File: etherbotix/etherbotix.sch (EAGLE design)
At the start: 107 parts, among them J1 J3011G21DNL, J2 22-03-5035, J3 22-03-5035, J4 22-03-5045, J5 22-03-5045, J6 1760510000, J7 1760490000, J8 502443-0470, J9 502443-0470, T1 TESTPAD, T2 TESTPAD, T3 TESTPAD, T4 TESTPAD, T5 TESTPAD, T6 TESTPAD, U1 STM32F407V, U2 TLK110, U3 OKI-78SR-5, U4 TLV1117, U5 ACS711ELCTR-25AB-T, U6 ACS711ELCTR-25AB-T, U7 MAX481CSA, U8 74LS126D, X1 25MHZ

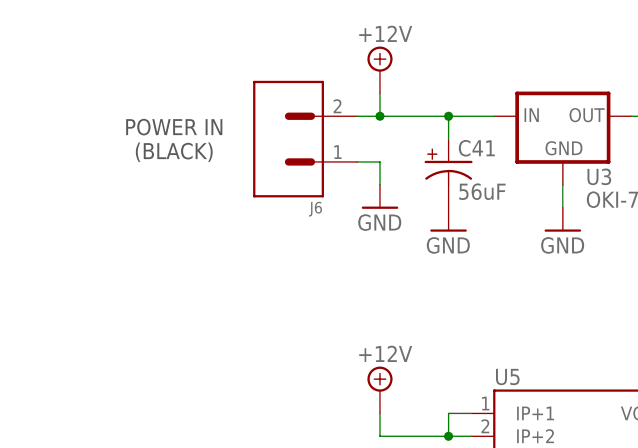
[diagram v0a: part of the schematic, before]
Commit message: add estop-capable 3-pin VIN header
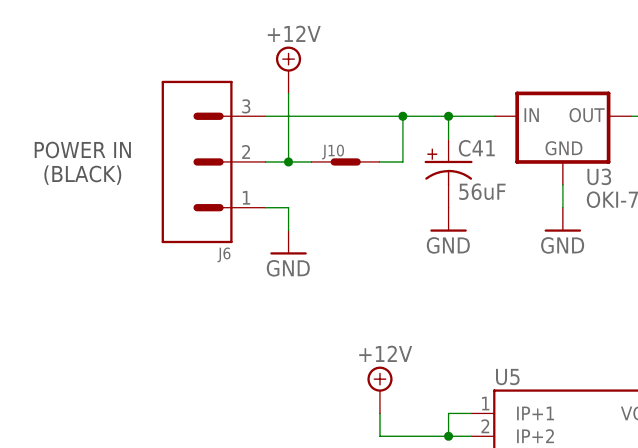
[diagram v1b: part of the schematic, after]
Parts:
- added J10: JUMPER, headers:JUMPER
- J6: value 1760510000 -> 1760520000; device headers:1760510000 -> headers:1760520000
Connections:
- new net N$29: C41.+, J10.B, J6.3, U3.IN
- net +12V: now also J10.A; no longer C41.+, U3.IN
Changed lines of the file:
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@@
 <part name="J4" library="molex" deviceset="22-03-5045" device=""/>
 <part name="J5" library="molex" deviceset="22-03-5045" device=""/>
-<part name="J6" library="headers" deviceset="1760510000" device=""/>
 <part name="J7" library="headers" deviceset="1760490000" device=""/>
 <part name="GND7" library="fergs" deviceset="GND" device=""/>
@@
 <part name="T5" library="fergs" deviceset="TESTPAD" device=""/>
 <part name="T6" library="fergs" deviceset="TESTPAD" device=""/>
+<part name="J6" library="headers" deviceset="1760520000" device=""/>
+<part name="J10" library="headers" deviceset="JUMPER" device=""/>
 </parts>
 <sheets>
 <sheet>
 <plain>
-<text x="15.24" y="205.74" size="1.778" layer="97" align="center">POWER IN
+<text x="5.08" y="203.2" size="1.778" layer="97" align="center">POWER IN
 (BLACK)</text>
 <text x="15.24" y="160.02" size="1.778" layer="97" align="center">AUX. OUT
@@
 <instance part="IMU" gate="G$1" x="314.96" y="25.4"/>
 <instance part="JTAG" gate="G$1" x="160.02" y="185.42"/>
-<instance part="SUPPLY1" gate="+12V" x="38.1" y="213.36"/>
+<instance part="SUPPLY1" gate="+12V" x="27.94" y="213.36"/>
 <instance part="SUPPLY2" gate="+5V" x="68.58" y="213.36"/>
 <instance part="SUPPLY3" gate="G$1" x="142.24" y="213.36"/>
-<instance part="GND1" gate="1" x="38.1" y="198.12"/>
+<instance part="GND1" gate="1" x="27.94" y="193.04"/>
 <instance part="GND2" gate="1" x="101.6" y="195.58"/>
 <instance part="GND3" gate="1" x="180.34" y="0"/>
@@
 <instance part="J4" gate="G$1" x="464.82" y="83.82"/>
 <instance part="J5" gate="G$1" x="495.3" y="83.82"/>
-<instance part="J6" gate="G$1" x="27.94" y="205.74" rot="R180"/>
 <instance part="J7" gate="G$1" x="27.94" y="160.02" rot="R180"/>
 <instance part="GND7" gate="1" x="58.42" y="195.58"/>
@@
 <instance part="T5" gate="G$1" x="325.12" y="154.94"/>
 <instance part="T6" gate="G$1" x="325.12" y="152.4"/>
+<instance part="J6" gate="G$1" x="17.78" y="203.2" rot="R180"/>
+<instance part="J10" gate="G$1" x="33.02" y="203.2"/>
 </instances>
 <busses>
@@
 <net name="+12V" class="0">
 <segment>
+<wire x1="25.4" y1="203.2" x2="27.94" y2="203.2" width="0.1524" layer="91"/>
+<pinref part="SUPPLY1" gate="+12V" pin="+12V"/>
+<wire x1="27.94" y1="203.2" x2="27.94" y2="210.82" width="0.1524" layer="91"/>
 <pinref part="J6" gate="G$1" pin="2"/>
-<pinref part="U3" gate="G$1" pin="IN"/>
-<wire x1="35.56" y1="208.28" x2="38.1" y2="208.28" width="0.1524" layer="91"/>
-<pinref part="SUPPLY1" gate="+12V" pin="+12V"/>
-<wire x1="38.1" y1="208.28" x2="45.72" y2="208.28" width="0.1524" layer="91"/>
-<wire x1="45.72" y1="208.28" x2="50.8" y2="208.28" width="0.1524" layer="91"/>
-<wire x1="38.1" y1="208.28" x2="38.1" y2="210.82" width="0.1524" layer="91"/>
-<junction x="38.1" y="208.28"/>
-<pinref part="C41" gate="G$1" pin="+"/>
-<wire x1="45.72" y1="205.74" x2="45.72" y2="208.28" width="0.1524" layer="91"/>
-<junction x="45.72" y="208.28"/>
+<wire x1="27.94" y1="203.2" x2="30.48" y2="203.2" width="0.1524" layer="91"/>
+<junction x="27.94" y="203.2"/>
+<pinref part="J10" gate="G$1" pin="A"/>
 </segment>
 <segment>
@@
 <net name="GND" class="0">
 <segment>
+<wire x1="25.4" y1="198.12" x2="27.94" y2="198.12" width="0.1524" layer="91"/>
+<wire x1="27.94" y1="198.12" x2="27.94" y2="195.58" width="0.1524" layer="91"/>
+<pinref part="GND1" gate="1" pin="GND"/>
 <pinref part="J6" gate="G$1" pin="1"/>
-<wire x1="35.56" y1="203.2" x2="38.1" y2="203.2" width="0.1524" layer="91"/>
-<wire x1="38.1" y1="203.2" x2="38.1" y2="200.66" width="0.1524" layer="91"/>
-<pinref part="GND1" gate="1" pin="GND"/>
 </segment>
 <segment>
@@
 </segment>
 </net>
+<net name="N$29" class="0">
+<segment>
+<pinref part="U3" gate="G$1" pin="IN"/>
+<wire x1="45.72" y1="208.28" x2="50.8" y2="208.28" width="0.1524" layer="91"/>
+<pinref part="C41" gate="G$1" pin="+"/>
+<wire x1="45.72" y1="205.74" x2="45.72" y2="208.28" width="0.1524" layer="91"/>
+<pinref part="J6" gate="G$1" pin="3"/>
+<wire x1="25.4" y1="208.28" x2="40.64" y2="208.28" width="0.1524" layer="91"/>
+<junction x="45.72" y="208.28"/>
+<wire x1="40.64" y1="208.28" x2="45.72" y2="208.28" width="0.1524" layer="91"/>
+<wire x1="40.64" y1="208.28" x2="40.64" y2="203.2" width="0.1524" layer="91"/>
+<junction x="40.64" y="208.28"/>
+<wire x1="40.64" y1="203.2" x2="38.1" y2="203.2" width="0.1524" layer="91"/>
+<pinref part="J10" gate="G$1" pin="B"/>
+</segment>
+</net>

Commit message: start rev. B
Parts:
- added T7, T8, T9: TESTPAD, fergs:TESTPAD
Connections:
- new net PE0: T7.1, U1.PE0(5T)
- new net PE1: T8.1, U1.PE1(5T)
- new net PE4: T9.1, U1.PE4(5T)
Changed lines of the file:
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@@
 <part name="J6" library="headers" deviceset="1760520000" device=""/>
 <part name="J10" library="headers" deviceset="JUMPER" device=""/>
+<part name="T7" library="fergs" deviceset="TESTPAD" device=""/>
+<part name="T8" library="fergs" deviceset="TESTPAD" device=""/>
+<part name="T9" library="fergs" deviceset="TESTPAD" device=""/>
 </parts>
 <sheets>
@@
 <instance part="J6" gate="G$1" x="17.78" y="203.2" rot="R180"/>
 <instance part="J10" gate="G$1" x="33.02" y="203.2"/>
+<instance part="T7" gate="G$1" x="325.12" y="114.3"/>
+<instance part="T8" gate="G$1" x="325.12" y="111.76"/>
+<instance part="T9" gate="G$1" x="325.12" y="104.14"/>
 </instances>
 <busses>
@@
 </segment>
 </net>
+<net name="PE4" class="0">
+<segment>
+<pinref part="U1" gate="G$1" pin="PE4(5T)"/>
+<pinref part="T9" gate="G$1" pin="1"/>
+<wire x1="322.58" y1="104.14" x2="317.5" y2="104.14" width="0.1524" layer="91"/>
+</segment>
+</net>
+<net name="PE1" class="0">
+<segment>
+<pinref part="U1" gate="G$1" pin="PE1(5T)"/>
+<pinref part="T8" gate="G$1" pin="1"/>
+<wire x1="322.58" y1="111.76" x2="317.5" y2="111.76" width="0.1524" layer="91"/>
+</segment>
+</net>
+<net name="PE0" class="0">
+<segment>
+<pinref part="U1" gate="G$1" pin="PE0(5T)"/>
+<pinref part="T7" gate="G$1" pin="1"/>
+<wire x1="322.58" y1="114.3" x2="317.5" y2="114.3" width="0.1524" layer="91"/>
+</segment>
+</net>

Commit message: add testpads to clocks, encoders, current sense
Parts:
- added T10, T11, T12, T13, T14, T15, T16, T17: TESTPAD, fergs:TESTPAD
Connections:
- net AUX_CURRENT_SENSE: now also T17.1
- net ETH_CLK: now also T10.1
- net M1_ENC_A: now also T12.1
- net M1_ENC_B: now also T13.1
- net M2_ENC_A: now also T14.1
- net M2_ENC_B: now also T15.1
- net N$15: now also T11.1
- net SERVO_CURRENT_SENSE: now also T16.1
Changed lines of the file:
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@@
 <part name="T8" library="fergs" deviceset="TESTPAD" device=""/>
 <part name="T9" library="fergs" deviceset="TESTPAD" device=""/>
+<part name="T10" library="fergs" deviceset="TESTPAD" device=""/>
+<part name="T11" library="fergs" deviceset="TESTPAD" device=""/>
+<part name="T12" library="fergs" deviceset="TESTPAD" device=""/>
+<part name="T13" library="fergs" deviceset="TESTPAD" device=""/>
+<part name="T14" library="fergs" deviceset="TESTPAD" device=""/>
+<part name="T15" library="fergs" deviceset="TESTPAD" device=""/>
+<part name="T16" library="fergs" deviceset="TESTPAD" device=""/>
+<part name="T17" library="fergs" deviceset="TESTPAD" device=""/>
 </parts>
 <sheets>
@@
 <instance part="T8" gate="G$1" x="325.12" y="111.76"/>
 <instance part="T9" gate="G$1" x="325.12" y="104.14"/>
+<instance part="T10" gate="G$1" x="55.88" y="119.38"/>
+<instance part="T11" gate="G$1" x="353.06" y="71.12"/>
+<instance part="T12" gate="G$1" x="365.76" y="195.58" rot="R180"/>
+<instance part="T13" gate="G$1" x="365.76" y="190.5" rot="R180"/>
+<instance part="T14" gate="G$1" x="365.76" y="157.48" rot="R180"/>
+<instance part="T15" gate="G$1" x="365.76" y="152.4" rot="R180"/>
+<instance part="T16" gate="G$1" x="515.62" y="121.92"/>
+<instance part="T17" gate="G$1" x="106.68" y="170.18"/>
 </instances>
 <busses>
@@
 <wire x1="73.66" y1="170.18" x2="104.14" y2="170.18" width="0.1524" layer="91"/>
 <label x="76.2" y="170.18" size="1.778" layer="95"/>
+<pinref part="T17" gate="G$1" pin="1"/>
 </segment>
 <segment>
@@
 <wire x1="477.52" y1="121.92" x2="513.08" y2="121.92" width="0.1524" layer="91"/>
 <label x="480.06" y="121.92" size="1.778" layer="95"/>
+<pinref part="T16" gate="G$1" pin="1"/>
 </segment>
 <segment>
@@
 <junction x="386.08" y="157.48"/>
 <pinref part="C18" gate="G$1" pin="1"/>
+<pinref part="T14" gate="G$1" pin="1"/>
 </segment>
 <segment>
@@
 <junction x="375.92" y="152.4"/>
 <pinref part="C17" gate="G$1" pin="1"/>
+<pinref part="T15" gate="G$1" pin="1"/>
 </segment>
 <segment>
@@
 <junction x="386.08" y="195.58"/>
 <pinref part="C13" gate="G$1" pin="1"/>
+<pinref part="T12" gate="G$1" pin="1"/>
 </segment>
 <segment>
@@
 <junction x="375.92" y="190.5"/>
 <pinref part="C4" gate="G$1" pin="1"/>
+<pinref part="T13" gate="G$1" pin="1"/>
 </segment>
 <segment>
@@
 <wire x1="347.98" y1="58.42" x2="347.98" y2="60.96" width="0.1524" layer="91"/>
 <junction x="347.98" y="60.96"/>
+<pinref part="T11" gate="G$1" pin="1"/>
+<wire x1="347.98" y1="71.12" x2="350.52" y2="71.12" width="0.1524" layer="91"/>
+<junction x="347.98" y="71.12"/>
 </segment>
 </net>
@@
 <wire x1="38.1" y1="119.38" x2="53.34" y2="119.38" width="0.1524" layer="91"/>
 <label x="40.64" y="119.38" size="1.778" layer="95"/>
-</segment>
-<segment>
+<pinref part="T10" gate="G$1" pin="1"/>
+</segment>
+<segment>

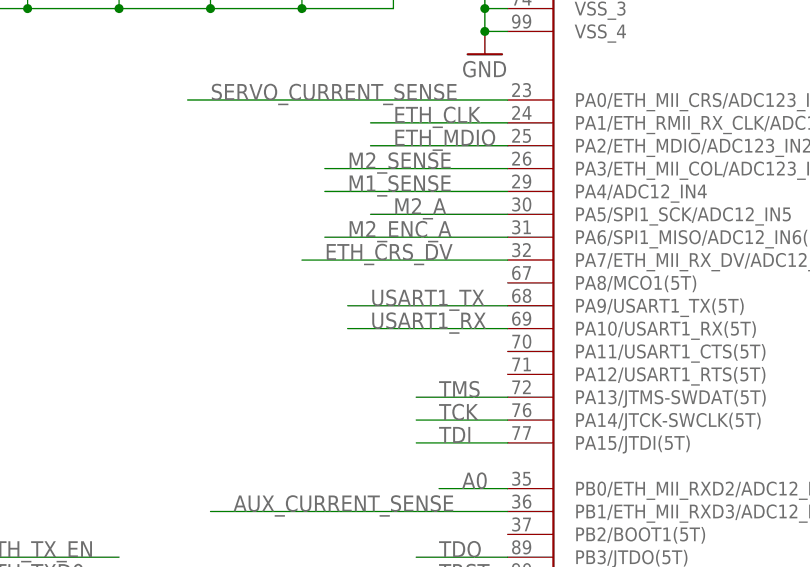
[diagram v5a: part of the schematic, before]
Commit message: add testpad for PA8 (mco1)
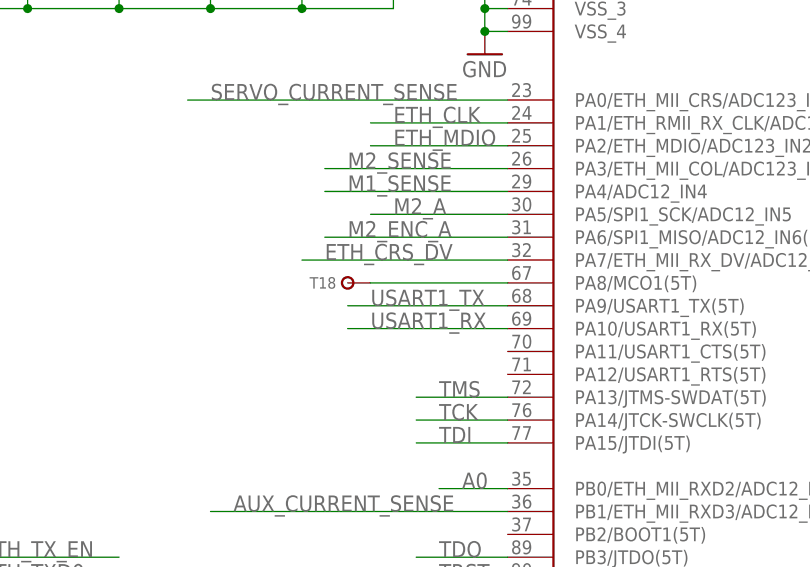
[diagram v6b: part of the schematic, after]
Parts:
- added T18: TESTPAD, fergs:TESTPAD
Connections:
- new net PA8: T18.1, U1.PA8/MCO1(5T)
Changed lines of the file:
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@@
 <part name="T16" library="fergs" deviceset="TESTPAD" device=""/>
 <part name="T17" library="fergs" deviceset="TESTPAD" device=""/>
+<part name="T18" library="fergs" deviceset="TESTPAD" device=""/>
 </parts>
 <sheets>
@@
 <instance part="T16" gate="G$1" x="515.62" y="121.92"/>
 <instance part="T17" gate="G$1" x="106.68" y="170.18"/>
+<instance part="T18" gate="G$1" x="220.98" y="119.38" rot="R180"/>
 </instances>
 <busses>
@@
 </segment>
 </net>
+<net name="PA8" class="0">
+<segment>
+<pinref part="T18" gate="G$1" pin="1"/>
+<pinref part="U1" gate="G$1" pin="PA8/MCO1(5T)"/>
+<wire x1="223.52" y1="119.38" x2="238.76" y2="119.38" width="0.1524" layer="91"/>
+</segment>
+</net>

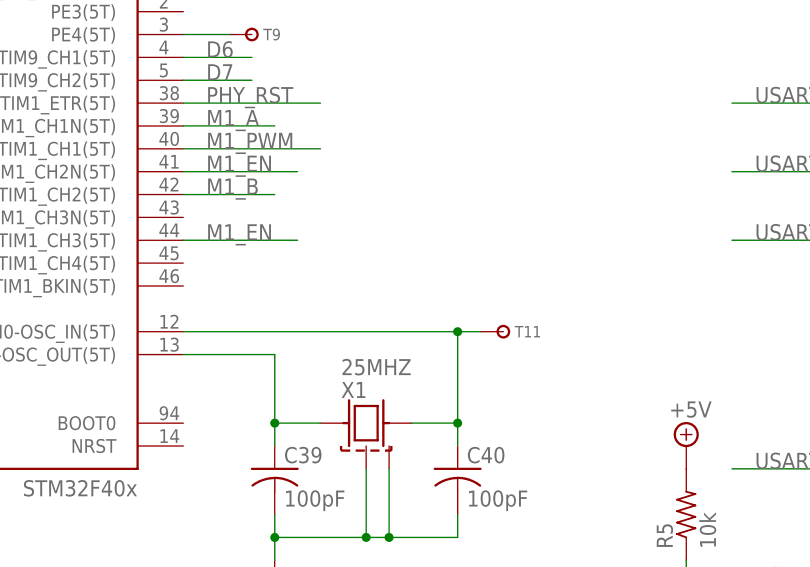
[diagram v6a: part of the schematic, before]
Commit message: add pin to force staying in bootloader
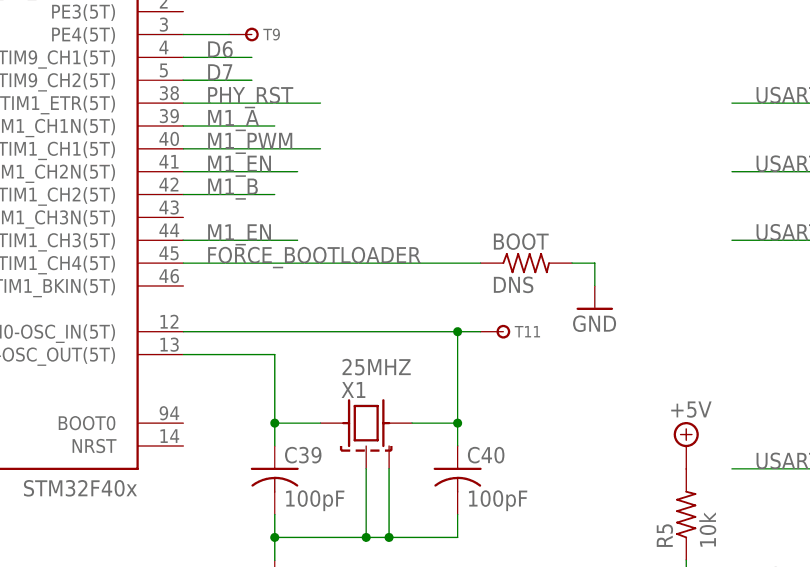
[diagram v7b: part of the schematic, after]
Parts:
- added BOOT: DNS, fergs:P1.00KHCT-ND
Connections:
- new net FORCE_BOOTLOADER: BOOT.1, U1.PE14/TIM1_CH4(5T)
- net GND: now also BOOT.2
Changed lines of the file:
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@@
 <part name="T17" library="fergs" deviceset="TESTPAD" device=""/>
 <part name="T18" library="fergs" deviceset="TESTPAD" device=""/>
+<part name="BOOT" library="fergs" deviceset="P1.00KHCT-ND" device="" value="DNS"/>
+<part name="GND61" library="fergs" deviceset="GND" device=""/>
 </parts>
 <sheets>
@@
 <instance part="T17" gate="G$1" x="106.68" y="170.18"/>
 <instance part="T18" gate="G$1" x="220.98" y="119.38" rot="R180"/>
+<instance part="BOOT" gate="G$1" x="355.6" y="78.74"/>
+<instance part="GND61" gate="1" x="363.22" y="73.66"/>
 </instances>
 <busses>
@@
 <pinref part="GND21" gate="1" pin="GND"/>
 <pinref part="R32" gate="G$1" pin="1"/>
+</segment>
+<segment>
+<pinref part="BOOT" gate="G$1" pin="2"/>
+<wire x1="360.68" y1="78.74" x2="363.22" y2="78.74" width="0.1524" layer="91"/>
+<wire x1="363.22" y1="78.74" x2="363.22" y2="76.2" width="0.1524" layer="91"/>
+<pinref part="GND61" gate="1" pin="GND"/>
 </segment>
 </net>
@@
 </segment>
 </net>
+<net name="FORCE_BOOTLOADER" class="0">
+<segment>
+<pinref part="U1" gate="G$1" pin="PE14/TIM1_CH4(5T)"/>
+<pinref part="BOOT" gate="G$1" pin="1"/>
+<wire x1="317.5" y1="78.74" x2="350.52" y2="78.74" width="0.1524" layer="91"/>
+<label x="320.04" y="78.74" size="1.778" layer="95"/>
+</segment>
+</net>
